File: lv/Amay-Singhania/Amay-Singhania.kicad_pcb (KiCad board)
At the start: 2 copper layers, 9.6 x 11.8 mm, 0 parts

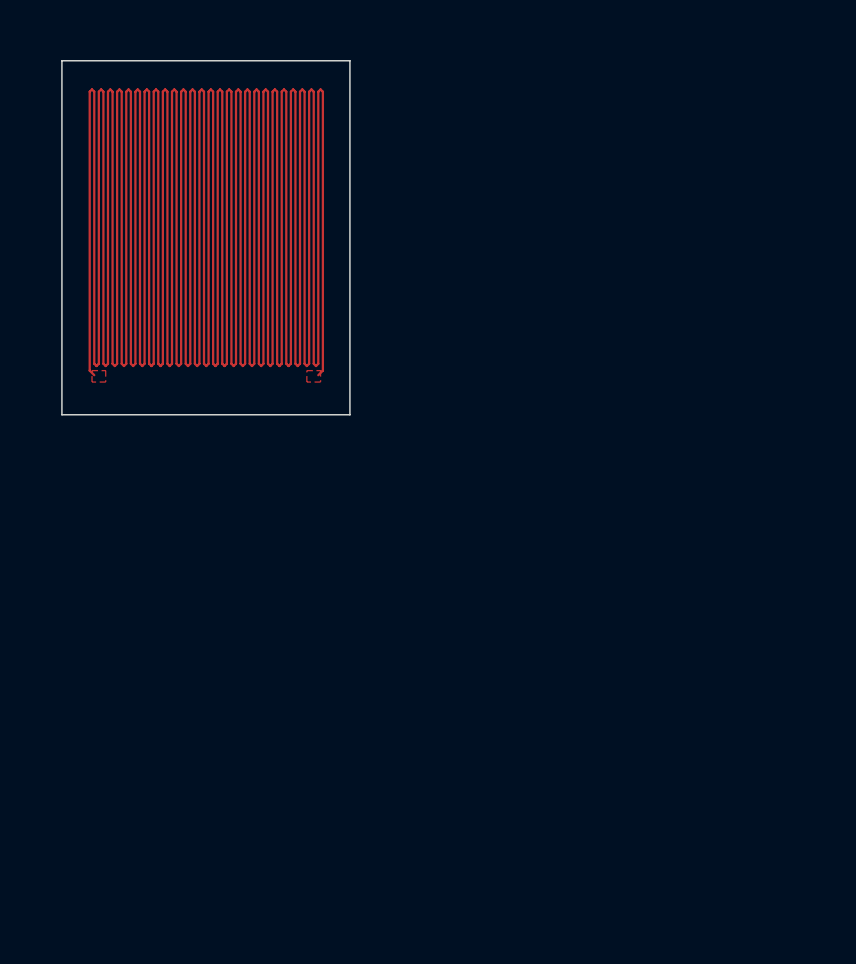
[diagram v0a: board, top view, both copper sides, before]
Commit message: created custom strain gauge footprint; added schematic with 1 reference gauge, 1 gauge, and 2 resistors as a wheatstone bridge; created pcb traces for gauge
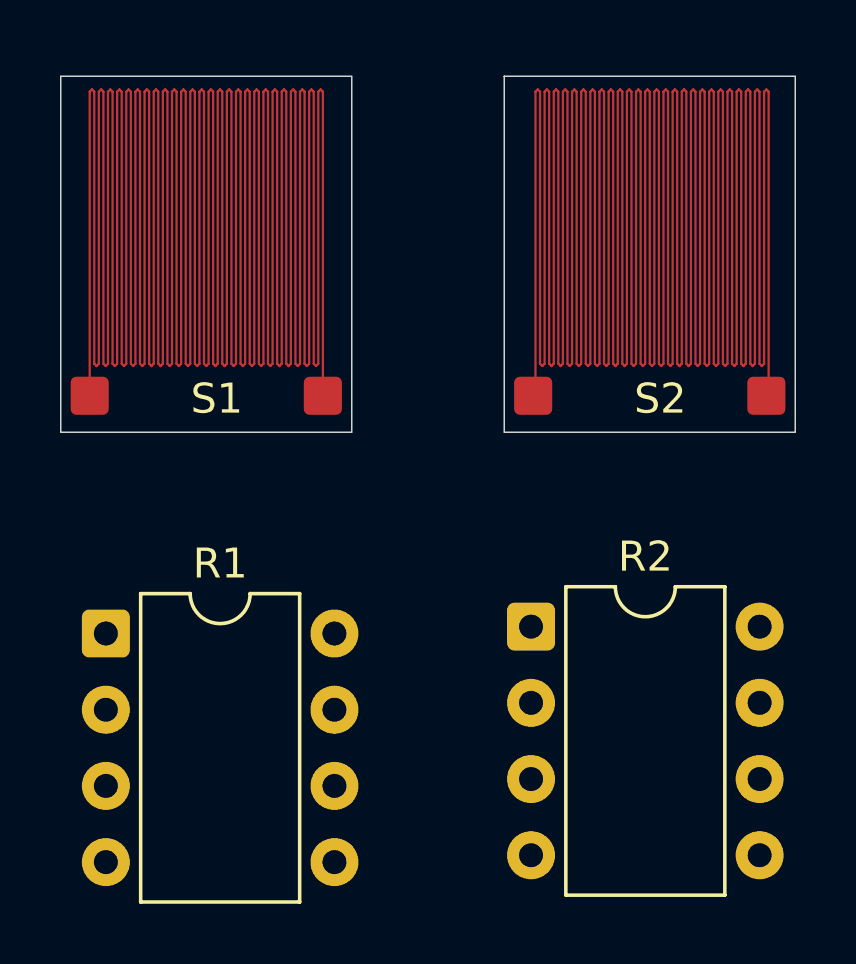
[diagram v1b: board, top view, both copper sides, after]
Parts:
- added R1: 350, Package_DIP:DIP-8_W7.62mm, F.Cu at (16.5, 47.1)
- added R2: 350, Package_DIP:DIP-8_W7.62mm, F.Cu at (30.6, 46.9)
- added S1: StrainGauge, StrainGuage:Strain Guage V1, F.Cu at (19.8, 39.2)
- added S2: StrainGaugeRef, StrainGuage:Strain Guage V1, F.Cu at (34.6, 39.2)
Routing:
- net +3.3V: track 0.00 -> 484.7 mm
- net (no net): track 483.4 -> 484.7 mm
- removed copper zone on F.Cu, net (none)
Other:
- board size 9.6 x 11.8 mm -> 9.7 x 11.9 mm

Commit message: edited kicad strain gauge footprint and changed the schematic
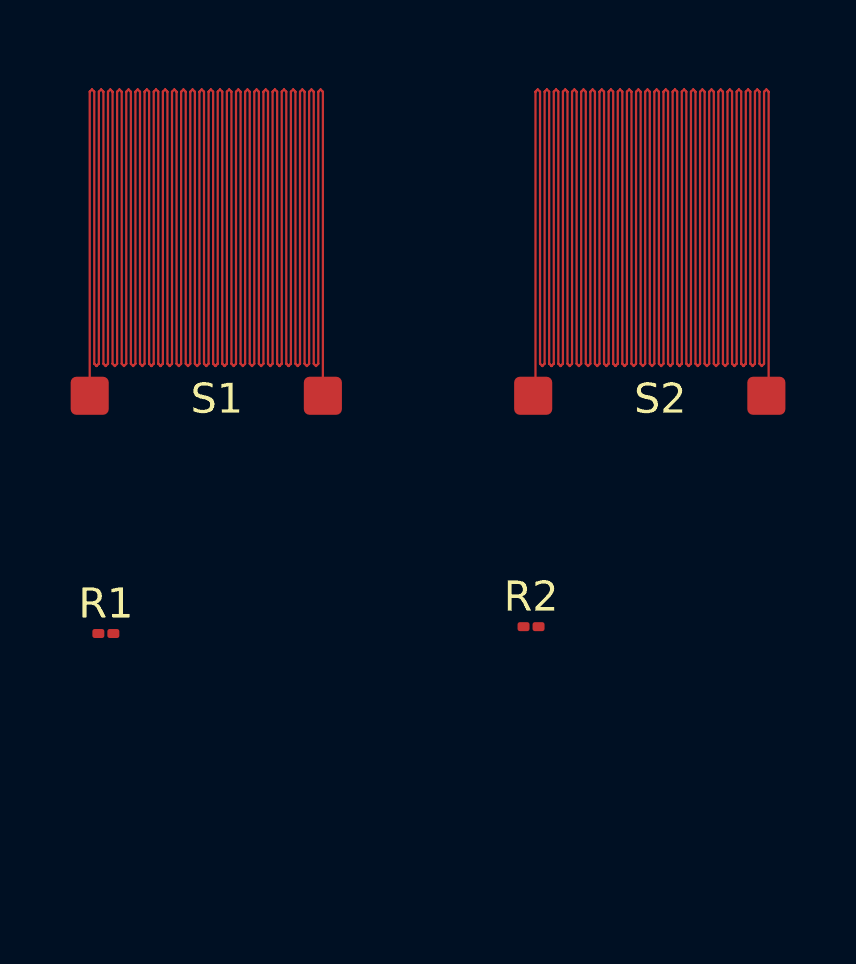
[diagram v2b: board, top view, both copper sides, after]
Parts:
- R1, R2: footprint Package_DIP:DIP-8_W7.62mm -> Resistor_SMD:R_01005_0402Metric
- S1, S2: footprint StrainGuage:Strain Guage V1 -> StrainGauge:Strain Gauge V1
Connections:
- net +3.3V renamed +3V3
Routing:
- net Net-(R1-Pad1): track 0.00 -> 484.7 mm
- net (no net): track 484.7 -> 0.00 mm
- net Net-(R2-Pad1): track 0.00 -> 484.7 mm
- net +3V3: track 484.7 -> 0.00 mm
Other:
- board outline removed
